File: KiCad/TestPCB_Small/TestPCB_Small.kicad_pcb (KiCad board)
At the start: 2 copper layers, 50.8 x 76.2 mm, 25 parts, among them U1 ESP32-S3-WROOM-1, U4 LSM6DSM

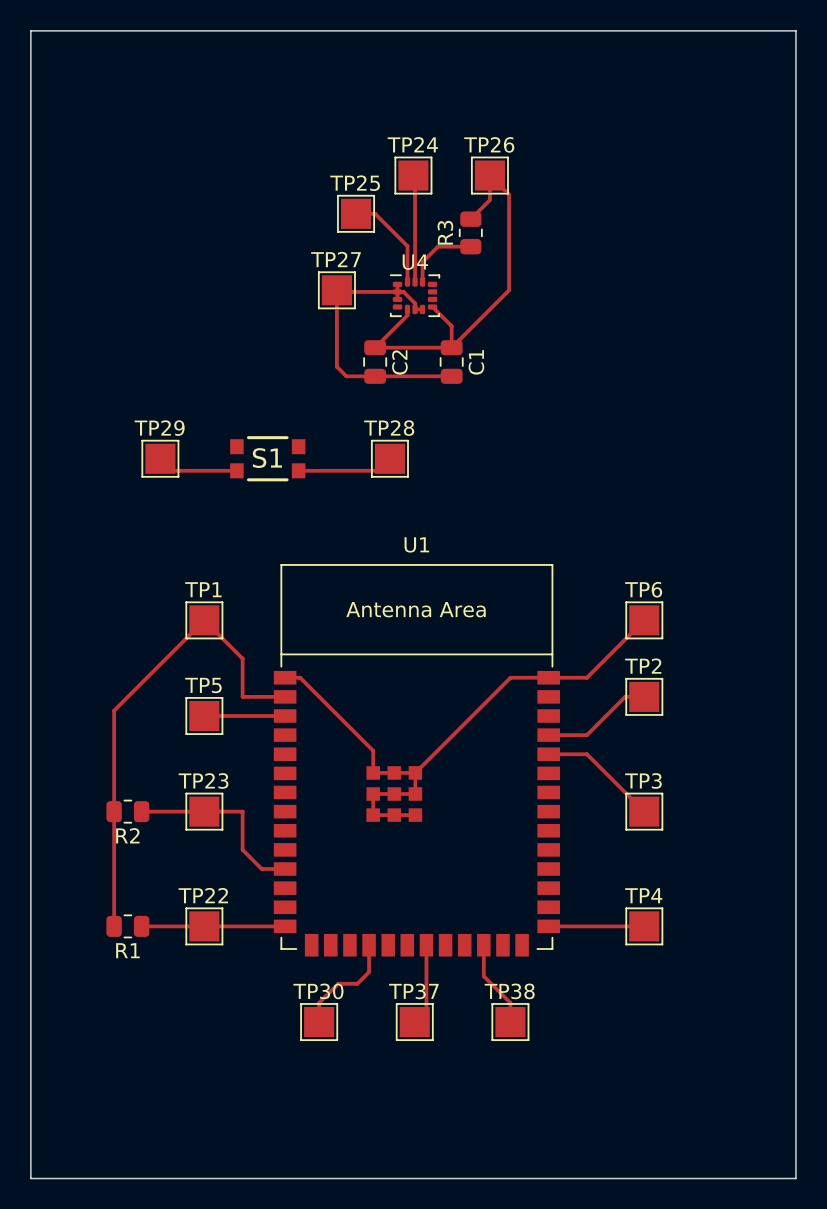
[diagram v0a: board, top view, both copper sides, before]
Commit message: CHG: pcb-layouts adopted
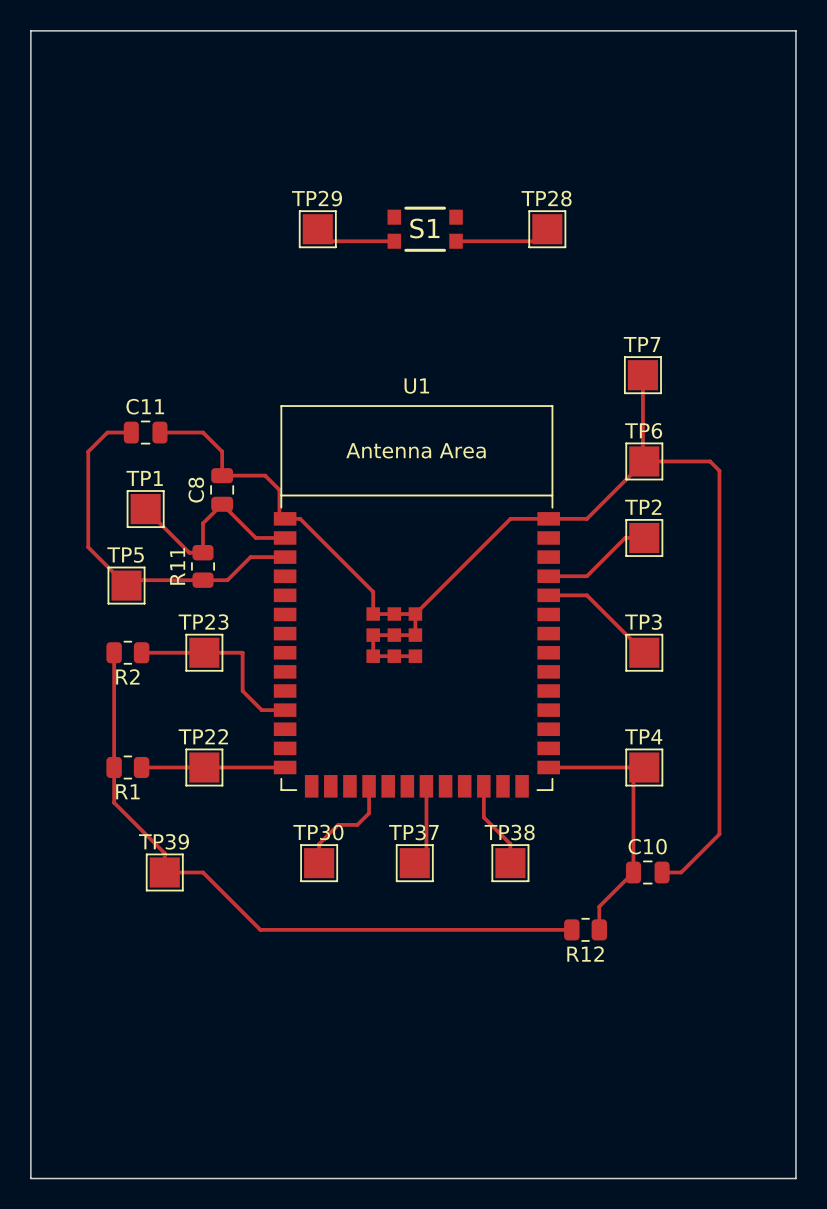
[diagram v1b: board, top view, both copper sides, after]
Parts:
- removed C1, C2: 100nF, Capacitor_SMD:C_0805_2012Metric
- removed R3: 10kΩ, Resistor_SMD:R_0805_2012Metric
- removed TP24: SCL, TestPoint:TestPoint_Pad_2.0x2.0mm
- removed TP25: SDA, TestPoint:TestPoint_Pad_2.0x2.0mm
- removed TP26: +3.3V, TestPoint:TestPoint_Pad_2.0x2.0mm
- removed TP27: GND, TestPoint:TestPoint_Pad_2.0x2.0mm
- removed U4: LSM6DSM, Package_LGA:LGA-14_3x2.5mm_P0.5mm_LayoutBorder3x4y
- added C10: 0.1µF, Capacitor_SMD:C_0805_2012Metric, F.Cu at (218.8, 106.7)
- added C11: 470nF, Capacitor_SMD:C_0805_2012Metric, F.Cu at (185.4, 77.5)
- added C8: 0.1µF, Capacitor_SMD:C_0805_2012Metric, F.Cu at (190.5, 81.3)
- added R11: 10kΩ, Resistor_SMD:R_0805_2012Metric, F.Cu at (189.2, 86.4)
- added R12: 10kΩ, Resistor_SMD:R_0805_2012Metric, F.Cu at (214.6, 110.5)
- added TP39: +3.3V, TestPoint:TestPoint_Pad_2.0x2.0mm, F.Cu at (186.7, 106.7)
- added TP7: FL_GND, TestPoint:TestPoint_Pad_2.0x2.0mm, F.Cu at (218.4, 73.7)
- moved TP28 18.5 mm to (212.1, 64.0)
- moved S1 18.5 mm to (204.0, 64.0)
- moved TP29 18.5 mm to (196.8, 64.0)
- moved R1 10.6 mm to (184.2, 99.7)
- moved TP22 10.6 mm to (189.3, 99.7)
- moved TP4 10.6 mm to (218.5, 99.7)
- moved U1 10.6 mm to (203.4, 91.5)
- moved R2 10.5 mm to (184.2, 92.1)
- moved TP2 10.5 mm to (218.5, 84.5)
- moved TP23 10.5 mm to (189.3, 92.1)
- moved TP3 10.5 mm to (218.5, 92.1)
- moved TP30 10.5 mm to (196.9, 106.1)
- moved TP37 10.5 mm to (203.3, 106.1)
- moved TP38 10.5 mm to (209.6, 106.1)
- moved TP6 10.5 mm to (218.5, 79.4)
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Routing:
- net Net-(C10-Pad2): track 39.9 -> 92.5 mm
- net Net-(U4-VDD): track 28.7 -> 0.00 mm
- net Net-(U1-3V3): track 31.8 -> 58.5 mm
- net Net-(U4-SCX): track 20.4 -> 0.00 mm
- net Net-(U1-EN): track 5.36 -> 24.6 mm
- net Net-(U1-GPIO0/BOOT): track 6.35 -> 18.4 mm
- net Net-(U4-SCL): track 7.11 -> 0.00 mm
- net Net-(U4-SDA): track 6.68 -> 0.00 mm
- net Net-(U4-CS): track 4.95 -> 0.00 mm

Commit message: CHG: changes of today
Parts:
- moved S1 5.55 mm to (204.0, 58.4)
- moved TP28 5.55 mm to (212.1, 58.4)
- moved TP29 5.55 mm to (196.8, 58.4)
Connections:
- S1 pad 1: Net-(S1-Pad1) -> unconnected-(S1-Pad1)
- S1 pad 4: unconnected-(S1-Pad4) -> Net-(S1-Pad4)
- TP29 pad 1: Net-(S1-Pad1) -> Net-(S1-Pad4)
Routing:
- net Net-(S1-Pad4): track 0.00 -> 5.41 mm
- net Net-(S1-Pad1): track 5.41 -> 0.00 mm
